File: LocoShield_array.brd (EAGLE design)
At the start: 128.3 x 106.7 mm, 103 parts, among them J1X11 0.100, J1X12 0.100, J1X21 0.100, J1X22 0.100, J2X11 RJ12/6, J2X12 RJ12/6, J2X21 RJ12/6, J2X22 RJ12/6, J3X11 RJ12/6, J3X12 RJ12/6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

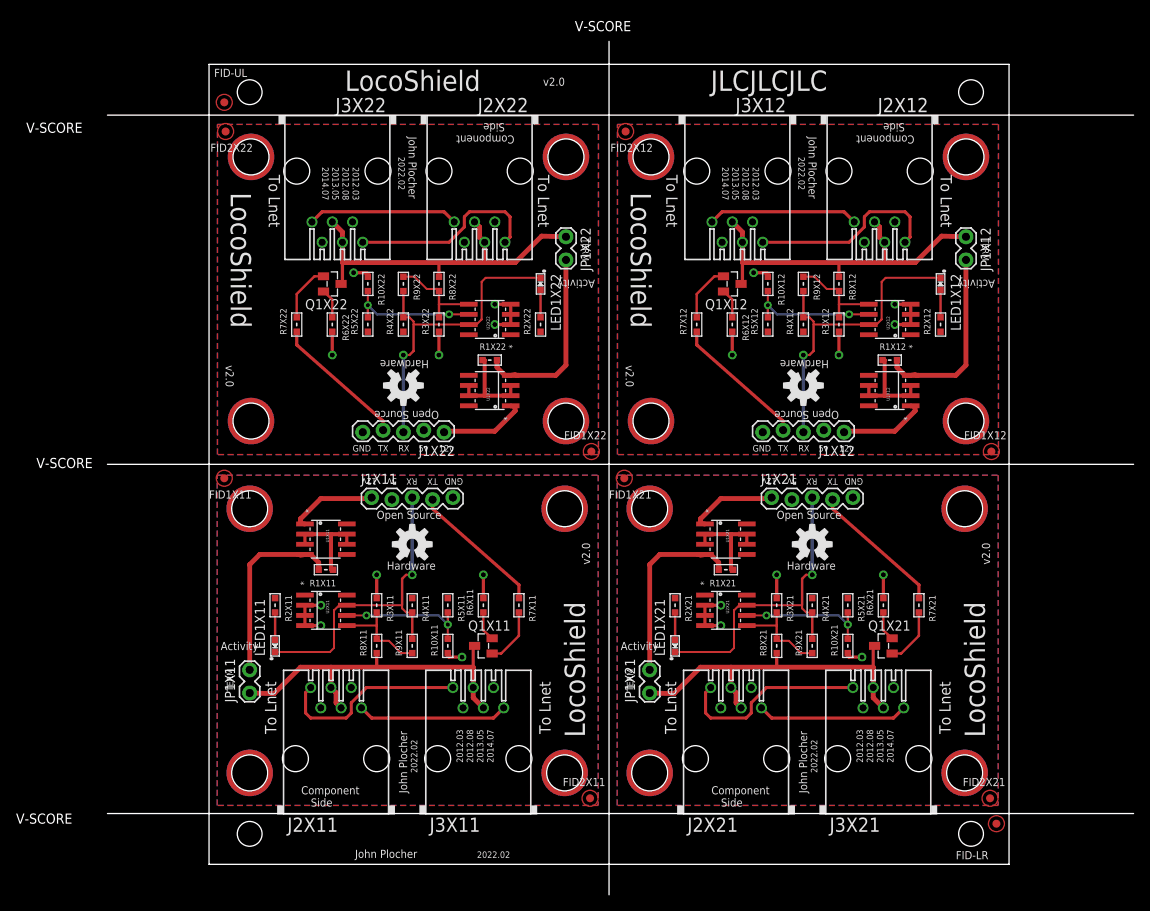
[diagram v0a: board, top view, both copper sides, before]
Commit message: vscore->mousebites
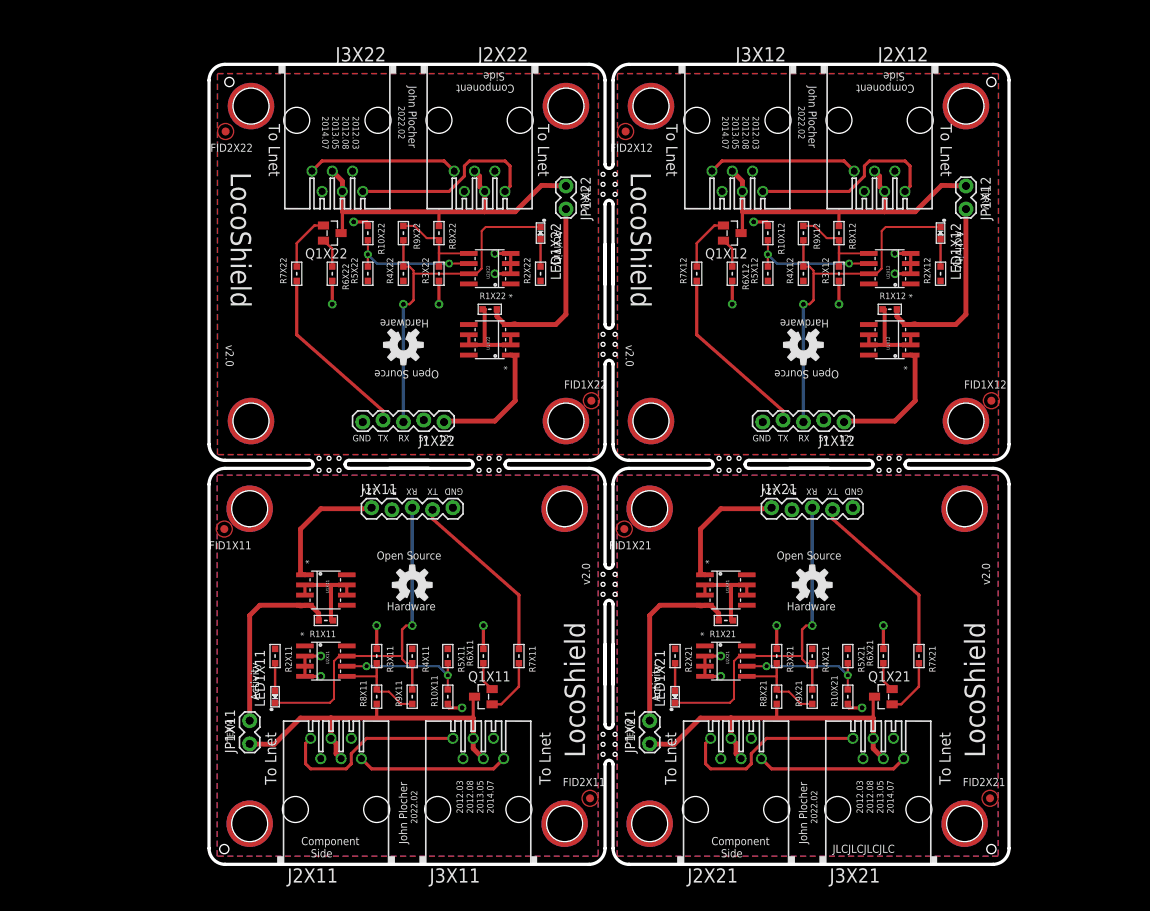
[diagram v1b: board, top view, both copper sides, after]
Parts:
- removed FID-LR, FID-UL: (no value), SPCoast:FIDUCIAL_1MM
- added U2X2, U2X3, U2X4, U2X5: (no value), SPCoast:MOUNTINGHOLE-TOOL
- U2X1: device SPCoast:BOARD-10X10-2X2-PANEL -> SPCoast:BOARD-10X10-2X2-PANEL-MB
- moved JP1X12 6.35 mm to (94.6, 84.6)
- moved JP1X22 6.35 mm to (44.6, 84.6)
- moved R2X12 6.35 mm to (91.4, 73.8)
- moved R2X22 6.35 mm to (41.4, 73.8)
- moved R3X12 6.35 mm to (78.7, 73.8)
- moved R3X22 6.35 mm to (28.7, 73.8)
- moved R4X12 6.35 mm to (74.3, 73.8)
- moved R4X22 6.35 mm to (24.3, 73.8)
- moved R5X12 6.35 mm to (69.8, 73.8)
- moved R5X22 6.35 mm to (19.9, 73.8)
- moved R6X12 6.35 mm to (65.4, 73.8)
- moved R6X22 6.35 mm to (15.4, 73.8)
- moved R7X12 6.35 mm to (61.0, 73.8)
- moved R7X22 6.35 mm to (11.0, 73.8)
- moved FID1X11 6.35 mm to (1.91, 41.9)
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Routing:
- net LNRXX12: track 40.6 -> 45.7 mm
- net LNRXX22: track 40.6 -> 45.7 mm
- net LNTXX22: track 17.2 -> 22.3 mm
- net LNTXX21: track 17.2 -> 22.3 mm
- net LNTXX12: track 17.2 -> 22.3 mm
- net LNTXX11: track 17.2 -> 22.3 mm
- net LNRXX11: track 40.6 -> 45.7 mm
- net V+X22: track 11.2 -> 16.3 mm
- net V+X21: track 11.2 -> 16.3 mm
- net V+X12: track 11.2 -> 16.3 mm
- net V+X11: track 11.2 -> 16.3 mm
- net LNRXX21: track 40.6 -> 45.7 mm
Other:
- board size 128.3 x 106.7 mm -> 100 x 100 mm
- board text added: "JLCJLCJLCJLC"
- board text removed: "JLCJLCJLC"
